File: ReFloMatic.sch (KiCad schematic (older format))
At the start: 33 parts, among them CON1 BARREL_JACK, P1 PROG, P2 THERMOCOUPLE, P3 DOOR_SERVO, P4 OVEN, Q1 MMUN2211, Q2 MMUN2111, Q3 MMUN2111, U1 STM32F030C, U2 MAX31855KASA

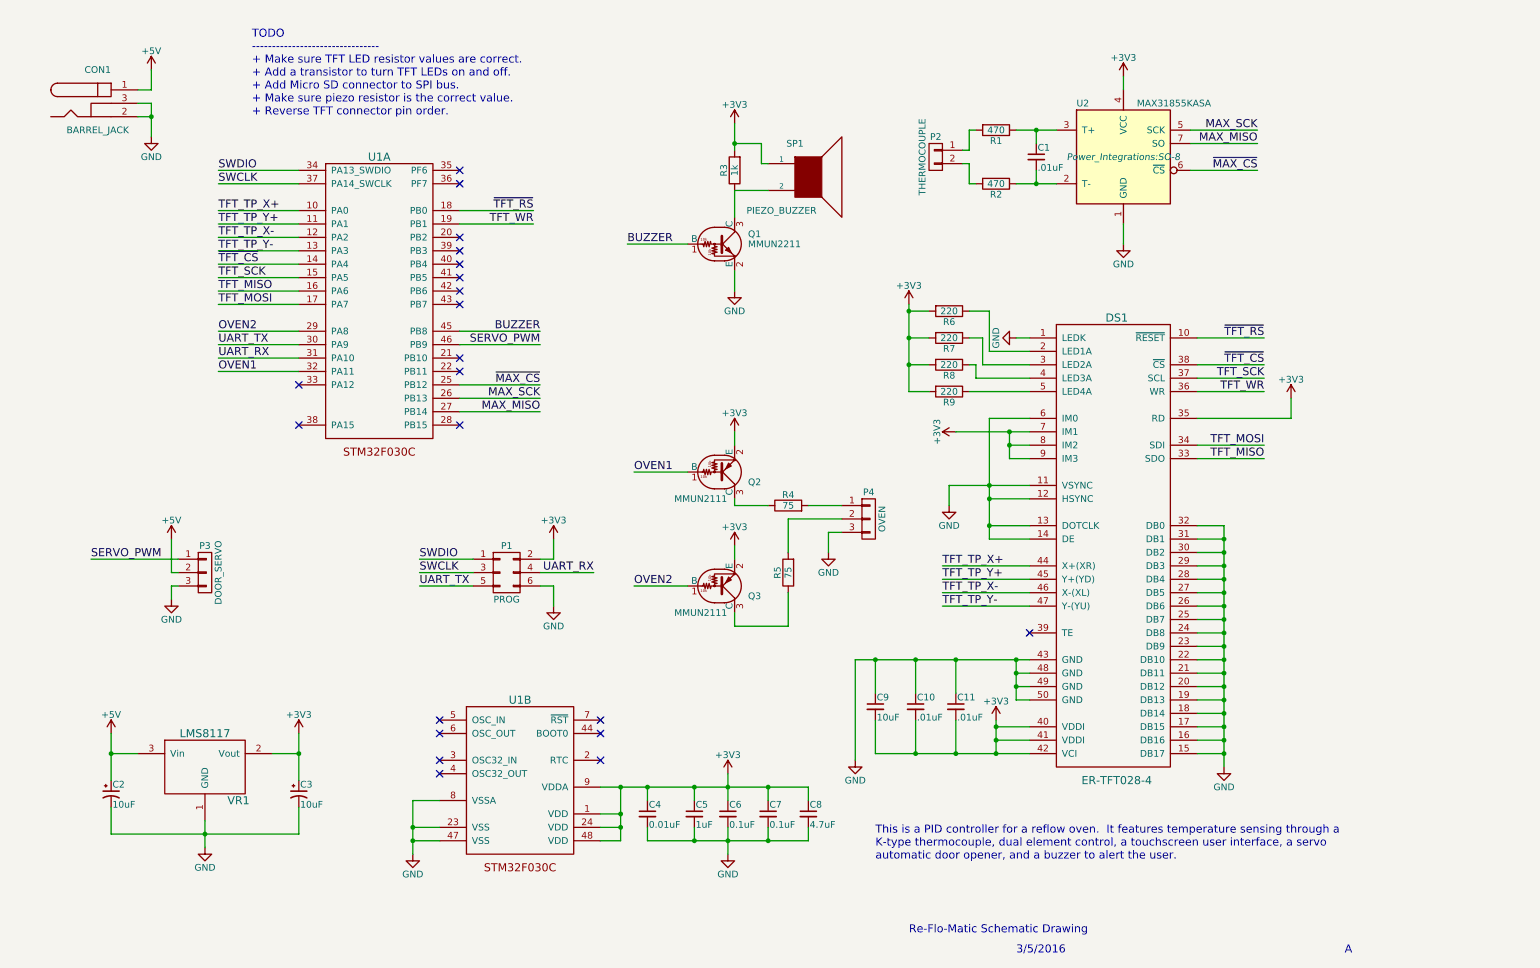
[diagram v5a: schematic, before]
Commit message: Added Micro SD card connector. Changed some component values. Began schematic rev B
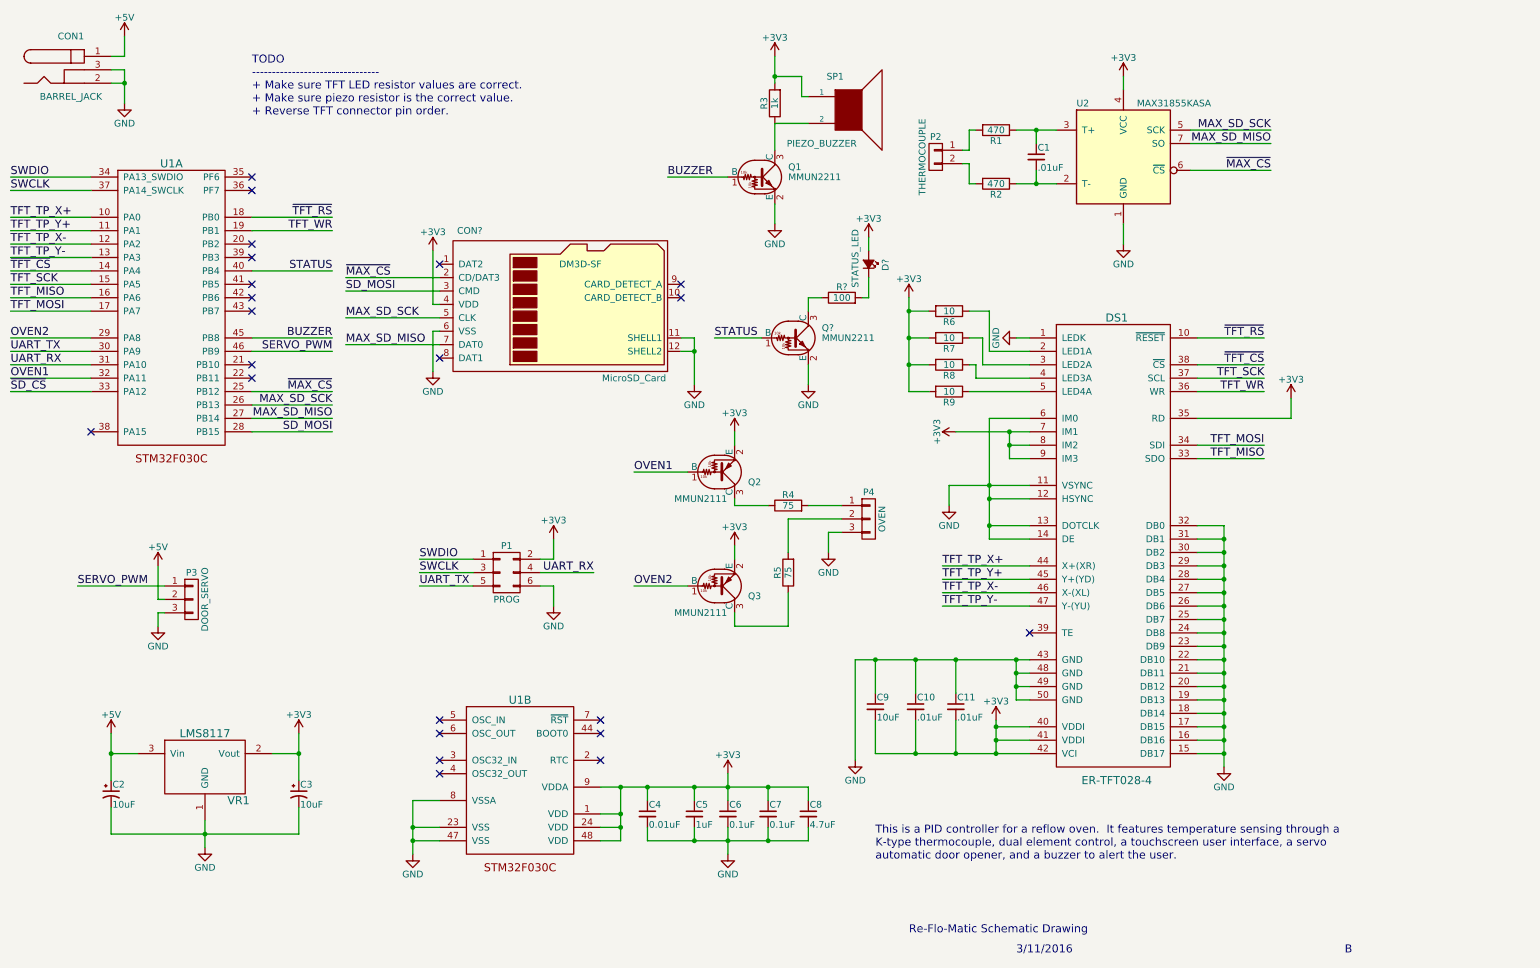
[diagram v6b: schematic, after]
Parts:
- added CON?: MicroSD_Card, DM3D-SF, symbol MicroSD_Card
- added D?: STATUS_LED, symbol Led_Small
- added Q?: MMUN2211, TO_SOT_Packages_SMD:SOT-23_Handsoldering, symbol DTC114E
- added R?: 100, Resistors_SMD:R_0805_HandSoldering, symbol R
- R6, R7, R8, R9: value 220 -> 10
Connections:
- net +3V3: now also CON?.4 (VDD), D?.2 (A)
- net GND: now also CON?.11 (SHELL1), CON?.12 (SHELL2), CON?.6 (VSS), Q?.2 (E)
- net ~MAX_CS: now also CON?.2 (CD/DAT3)
- net SD_MOSI: now reaches U1.28 (PB15)
- net SD_MOSI: now also CON?.3 (CMD)
- net ~SD_CS: now reaches U1.33 (PA12)
- net STATUS: now reaches U1.40 (PB4)
- net STATUS: now also Q?.1 (B)
- net MAX_MISO renamed MAX_SD_MISO
- net MAX_SD_MISO: now also CON?.7 (DAT0)
- net MAX_SCK renamed MAX_SD_SCK
- net MAX_SD_SCK: now also CON?.5 (CLK)
- new net: Q?.3 (C), R?.1
- new net: D?.1 (K), R?.2
- no-connect marks 21 -> 22
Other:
- note added: "3/11/2016"
- note added: "B"
- note added: "TODO\n--------------------------------\n+ Make sure TFT LED resistor values are correct.\n+ Make sure piezo resistor is the correct value.\n+ Reverse TFT connector pin order."
- note removed: "3/5/2016"
- note removed: "A"
- note removed: "TODO\n--------------------------------\n+ Make sure TFT LED resistor values are correct.\n+ Add a transistor to turn TFT LEDs on and off.\n+ Add Micro SD connector to SPI bus.\n+ Make sure piezo resistor is the correct value.\n+ Reverse TFT connector pin order."
- moved on the sheet: CON1, P3, Q1, R3, SP1, U1A

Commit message: Finished Rev. B of schematic.
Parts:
- added R? (x2): 47k, Resistors_SMD:R_0805_HandSoldering, symbol R
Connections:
- net +3V3: now also R?.1, R?.2
- net at CON?.1 (DAT2): now also R?.1
- net at CON?.8 (DAT1): now also R?.2
- no-connect marks 22 -> 20
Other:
- note added: "This is a PID controller for a reflow oven. It features temperature sensing through a\nK-type thermocouple, dual element control, a touchscreen user interface, a servo\nautomatic door opener, a Micro SD slot for storing icons used in the UI and storing\ntemperature profiles, and a buzzer to alert the user."
- note removed: "TODO\n--------------------------------\n+ Make sure TFT LED resistor values are correct.\n+ Make sure piezo resistor is the correct value.\n+ Reverse TFT connector pin order."
- note removed: "This is a PID controller for a reflow oven. It features temperature sensing through a\nK-type thermocouple, dual element control, a touchscreen user interface, a servo\nautomatic door opener, and a buzzer to alert the user."
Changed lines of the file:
@@
 	1    0    0    -1
 $EndComp
-Text Notes 7100 6950 0    60   ~ 0
-This is a PID controller for a reflow oven.  It features temperature sensing through a\nK-type thermocouple, dual element control, a touchscreen user interface, a servo\nautomatic door opener, and a buzzer to alert the user.
+Text Notes 7100 7000 0    60   ~ 0
+This is a PID controller for a reflow oven.  It features temperature sensing through a\nK-type thermocouple, dual element control, a touchscreen user interface, a servo\nautomatic door opener, a Micro SD slot for storing icons used in the UI and storing\ntemperature profiles, and a buzzer to alert the user.
 Text Notes 7350 7500 0    60   ~ 0
 Re-Flo-Matic Schematic Drawing
@@
 Text Notes 10600 7650 0    60   ~ 0
 B
-Text Notes 2450 1400 0    60   ~ 0
-TODO\n--------------------------------\n+ Make sure TFT LED resistor values are correct.\n+ Make sure piezo resistor is the correct value.\n+ Reverse TFT connector pin order.
 Text Label 3050 3750 2    60   ~ 0
 SD_MOSI
@@
 Wire Wire Line
 	3150 2600 3850 2600
-NoConn ~ 3850 2500
 Wire Wire Line
 	3150 3100 3850 3100
-NoConn ~ 3850 3200
 $Comp
 L GND #PWR?
@@
 L +3V3 #PWR?
 U 1 1 56E50399
-P 3800 2400
-F 0 "#PWR?" H 3800 2250 50  0001 C CNN
-F 1 "+3V3" H 3800 2540 50  0000 C CNN
-F 2 "" H 3800 2400 50  0000 C CNN
-F 3 "" H 3800 2400 50  0000 C CNN
-	1    3800 2400
-	1    0    0    -1
-$EndComp
-Wire Wire Line
-	3800 2400 3800 2800
+P 3700 2000
+F 0 "#PWR?" H 3700 1850 50  0001 C CNN
+F 1 "+3V3" H 3700 2140 50  0000 C CNN
+F 2 "" H 3700 2000 50  0000 C CNN
+F 3 "" H 3700 2000 50  0000 C CNN
+	1    3700 2000
+	1    0    0    -1
+$EndComp
+Wire Wire Line
+	3800 2050 3800 2800
 Wire Wire Line
 	3800 2800 3850 2800
+$Comp
+L R R?
+U 1 1 56E5D162
+P 3600 2250
+F 0 "R?" V 3680 2250 50  0000 C CNN
+F 1 "47k" V 3600 2250 50  0000 C CNN
+F 2 "Resistors_SMD:R_0805_HandSoldering" V 3530 2250 50  0001 C CNN
+F 3 "" H 3600 2250 50  0000 C CNN
+	1    3600 2250
+	-1   0    0    1
+$EndComp
+Wire Wire Line
+	3850 2500 3600 2500
+Wire Wire Line
+	3600 2500 3600 2400
+Wire Wire Line
+	3600 2100 3600 2050
+Wire Wire Line
+	3600 2050 3800 2050
+Wire Wire Line
+	3700 2050 3700 2000
+Connection ~ 3700 2050
+$Comp
+L R R?
+U 1 1 56E5D7B9
+P 3500 3250
+F 0 "R?" V 3580 3250 50  0000 C CNN
+F 1 "47k" V 3500 3250 50  0000 C CNN
+F 2 "Resistors_SMD:R_0805_HandSoldering" V 3430 3250 50  0001 C CNN
+F 3 "" H 3500 3250 50  0000 C CNN
+	1    3500 3250
+	0    -1   -1   0
+$EndComp
+$Comp
+L +3V3 #PWR?
+U 1 1 56E5D887
+P 3300 3250
+F 0 "#PWR?" H 3300 3100 50  0001 C CNN
+F 1 "+3V3" H 3300 3390 50  0000 C CNN
+F 2 "" H 3300 3250 50  0000 C CNN
+F 3 "" H 3300 3250 50  0000 C CNN
+	1    3300 3250
+	0    -1   -1   0
+$EndComp
+Wire Wire Line
+	3350 3250 3300 3250
+Wire Wire Line
+	3650 3250 3700 3250
+Wire Wire Line
+	3700 3250 3700 3200
+Wire Wire Line
+	3700 3200 3850 3200
 $EndSCHEMATC

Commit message: Painstakingly created micro sd card footprint and 3D model to match.
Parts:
- C1, C10, C11, C4, C5, C6, C7: footprint Capacitors_SMD:C_0805_HandSoldering -> Capacitors_SMD:C_0805
- CON2: renamed from CON?; footprint DM3D-SF -> SD:DM3D-SF
- D1: renamed from D?; footprint (none) -> LEDs:LED_0805
- DS1: footprint (none) -> TFT:FPC_50
- Q1, Q2, Q3: footprint TO_SOT_Packages_SMD:SOT-23_Handsoldering -> TO_SOT_Packages_SMD:SOT-23
- Q4: renamed from Q?; footprint TO_SOT_Packages_SMD:SOT-23_Handsoldering -> TO_SOT_Packages_SMD:SOT-23
- R1, R2, R3, R4, R5, R6, R7, R8, R9: footprint Resistors_SMD:R_0805_HandSoldering -> Resistors_SMD:R_0805
- R10, R11, R12: renamed from R?; footprint Resistors_SMD:R_0805_HandSoldering -> Resistors_SMD:R_0805
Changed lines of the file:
@@
 F 0 "C1" H 8310 1770 50  0000 L CNN
 F 1 ".01uF" H 8310 1620 50  0000 L CNN
-F 2 "Capacitors_SMD:C_0805_HandSoldering" H 8300 1700 50  0001 C CNN
+F 2 "Capacitors_SMD:C_0805" H 8300 1700 50  0001 C CNN
 F 3 "" H 8300 1700 50  0000 C CNN
 	1    8300 1700
@@
 F 0 "R1" V 8080 1500 50  0000 C CNN
 F 1 "470" V 8000 1500 50  0000 C CNN
-F 2 "Resistors_SMD:R_0805_HandSoldering" V 7930 1500 50  0001 C CNN
+F 2 "Resistors_SMD:R_0805" V 7930 1500 50  0001 C CNN
 F 3 "" H 8000 1500 50  0000 C CNN
 	1    8000 1500
@@
 F 0 "R2" V 8080 1900 50  0000 C CNN
 F 1 "470" V 8000 1900 50  0000 C CNN
-F 2 "Resistors_SMD:R_0805_HandSoldering" V 7930 1900 50  0001 C CNN
+F 2 "Resistors_SMD:R_0805" V 7930 1900 50  0001 C CNN
 F 3 "" H 8000 1900 50  0000 C CNN
 	1    8000 1900
@@
 F 0 "DS1" H 8900 6300 60  0000 C CNN
 F 1 "ER-TFT028-4" H 8900 2850 60  0000 C CNN
-F 2 "" H 8850 6300 60  0001 C CNN
+F 2 "TFT:FPC_50" H 8850 6300 60  0001 C CNN
 F 3 "" H 8850 6300 60  0000 C CNN
 	1    8900 4600
@@
 F 0 "R6" V 7730 2850 50  0000 C CNN
 F 1 "10" V 7650 2850 50  0000 C CNN
-F 2 "Resistors_SMD:R_0805_HandSoldering" V 7580 2850 50  0001 C CNN
+F 2 "Resistors_SMD:R_0805" V 7580 2850 50  0001 C CNN
 F 3 "" H 7650 2850 50  0000 C CNN
 	1    7650 2850
@@
 F 0 "R7" V 7730 3050 50  0000 C CNN
 F 1 "10" V 7650 3050 50  0000 C CNN
-F 2 "Resistors_SMD:R_0805_HandSoldering" V 7580 3050 50  0001 C CNN
+F 2 "Resistors_SMD:R_0805" V 7580 3050 50  0001 C CNN
 F 3 "" H 7650 3050 50  0000 C CNN
 	1    7650 3050
@@
 F 0 "R8" V 7730 3250 50  0000 C CNN
 F 1 "10" V 7650 3250 50  0000 C CNN
-F 2 "Resistors_SMD:R_0805_HandSoldering" V 7580 3250 50  0001 C CNN
+F 2 "Resistors_SMD:R_0805" V 7580 3250 50  0001 C CNN
 F 3 "" H 7650 3250 50  0000 C CNN
 	1    7650 3250
@@
 F 0 "R9" V 7730 3450 50  0000 C CNN
 F 1 "10" V 7650 3450 50  0000 C CNN
-F 2 "Resistors_SMD:R_0805_HandSoldering" V 7580 3450 50  0001 C CNN
+F 2 "Resistors_SMD:R_0805" V 7580 3450 50  0001 C CNN
 F 3 "" H 7650 3450 50  0000 C CNN
 	1    7650 3450
@@
 F 0 "C11" H 7710 5870 50  0000 L CNN
 F 1 ".01uF" H 7710 5720 50  0000 L CNN
-F 2 "Capacitors_SMD:C_0805_HandSoldering" H 7700 5800 50  0001 C CNN
+F 2 "Capacitors_SMD:C_0805" H 7700 5800 50  0001 C CNN
 F 3 "" H 7700 5800 50  0000 C CNN
 	1    7700 5800
@@
 F 0 "C10" H 7410 5870 50  0000 L CNN
 F 1 ".01uF" H 7410 5720 50  0000 L CNN
-F 2 "Capacitors_SMD:C_0805_HandSoldering" H 7400 5800 50  0001 C CNN
+F 2 "Capacitors_SMD:C_0805" H 7400 5800 50  0001 C CNN
 F 3 "" H 7400 5800 50  0000 C CNN
 	1    7400 5800
@@
 F 0 "R3" V 6430 1300 50  0000 C CNN
 F 1 "1k" V 6350 1300 50  0000 C CNN
-F 2 "Resistors_SMD:R_0805_HandSoldering" V 6280 1300 50  0001 C CNN
+F 2 "Resistors_SMD:R_0805" V 6280 1300 50  0001 C CNN
 F 3 "" H 6350 1300 50  0000 C CNN
 	1    6350 1300
@@
 F 0 "R4" V 6530 4300 50  0000 C CNN
 F 1 "75" V 6450 4300 50  0000 C CNN
-F 2 "Resistors_SMD:R_0805_HandSoldering" V 6380 4300 50  0001 C CNN
+F 2 "Resistors_SMD:R_0805" V 6380 4300 50  0001 C CNN
 F 3 "" H 6450 4300 50  0000 C CNN
 	1    6450 4300
@@
 F 0 "R5" V 6530 4800 50  0000 C CNN
 F 1 "75" V 6450 4800 50  0000 C CNN
-F 2 "Resistors_SMD:R_0805_HandSoldering" V 6380 4800 50  0001 C CNN
+F 2 "Resistors_SMD:R_0805" V 6380 4800 50  0001 C CNN
 F 3 "" H 6450 4800 50  0000 C CNN
 	1    6450 4800
@@
 F 0 "C4" H 5410 6670 50  0000 L CNN
 F 1 "0.01uF" H 5410 6520 50  0000 L CNN
-F 2 "Capacitors_SMD:C_0805_HandSoldering" H 5400 6600 50  0001 C CNN
+F 2 "Capacitors_SMD:C_0805" H 5400 6600 50  0001 C CNN
 F 3 "" H 5400 6600 50  0000 C CNN
 	1    5400 6600
@@
 F 0 "C5" H 5760 6670 50  0000 L CNN
 F 1 "1uF" H 5760 6520 50  0000 L CNN
-F 2 "Capacitors_SMD:C_0805_HandSoldering" H 5750 6600 50  0001 C CNN
+F 2 "Capacitors_SMD:C_0805" H 5750 6600 50  0001 C CNN
 F 3 "" H 5750 6600 50  0000 C CNN
 	1    5750 6600
@@
 F 0 "C6" H 6010 6670 50  0000 L CNN
 F 1 "0.1uF" H 6010 6520 50  0000 L CNN
-F 2 "Capacitors_SMD:C_0805_HandSoldering" H 6000 6600 50  0001 C CNN
+F 2 "Capacitors_SMD:C_0805" H 6000 6600 50  0001 C CNN
 F 3 "" H 6000 6600 50  0000 C CNN
 	1    6000 6600
@@
 F 0 "C7" H 6310 6670 50  0000 L CNN
 F 1 "0.1uF" H 6310 6520 50  0000 L CNN
-F 2 "Capacitors_SMD:C_0805_HandSoldering" H 6300 6600 50  0001 C CNN
+F 2 "Capacitors_SMD:C_0805" H 6300 6600 50  0001 C CNN
 F 3 "" H 6300 6600 50  0000 C CNN
 	1    6300 6600
@@
 F 0 "Q1" H 6450 1925 50  0000 L CNN
 F 1 "MMUN2211" H 6450 1850 50  0000 L CNN
-F 2 "TO_SOT_Packages_SMD:SOT-23_Handsoldering" H 6250 1850 50  0001 L CNN
+F 2 "TO_SOT_Packages_SMD:SOT-23" H 6250 1850 50  0001 L CNN
 F 3 "" H 6250 1850 50  0000 L CNN
 	1    6250 1850
@@
 F 0 "Q2" H 6150 4125 50  0000 L CNN
 F 1 "MMUN2111" H 5600 4250 50  0000 L CNN
-F 2 "TO_SOT_Packages_SMD:SOT-23_Handsoldering" H 5950 4050 50  0001 L CNN
+F 2 "TO_SOT_Packages_SMD:SOT-23" H 5950 4050 50  0001 L CNN
 F 3 "" H 5950 4050 50  0000 L CNN
 	1    5950 4050
@@
 F 0 "Q3" H 6150 4975 50  0000 L CNN
 F 1 "MMUN2111" H 5600 5100 50  0000 L CNN
-F 2 "TO_SOT_Packages_SMD:SOT-23_Handsoldering" H 5950 4900 50  0001 L CNN
+F 2 "TO_SOT_Packages_SMD:SOT-23" H 5950 4900 50  0001 L CNN
 F 3 "" H 5950 4900 50  0000 L CNN
 	1    5950 4900
@@
 	650  3450 1250 3450
 $Comp
-L MicroSD_Card CON?
+L MicroSD_Card CON2
 U 1 1 56E3F832
 P 4750 2900
-F 0 "CON?" H 4075 3550 50  0000 C CNN
+F 0 "CON2" H 4075 3550 50  0000 C CNN
 F 1 "MicroSD_Card" H 5300 2450 50  0000 C CNN
-F 2 "DM3D-SF" H 4900 3300 50  0000 C CNN
+F 2 "SD:DM3D-SF" H 4900 3300 50  0001 C CNN
 F 3 "" H 4750 2900 50  0000 C CNN
 	1    4750 2900
@@
 $EndComp
 $Comp
-L DTC114E Q?
+L DTC114E Q4
 U 1 1 56E48E99
 P 6500 3050
-F 0 "Q?" H 6700 3125 50  0000 L CNN
+F 0 "Q4" H 6700 3125 50  0000 L CNN
 F 1 "MMUN2211" H 6700 3050 50  0000 L CNN
-F 2 "TO_SOT_Packages_SMD:SOT-23_Handsoldering" H 6500 3050 50  0001 L CNN
+F 2 "TO_SOT_Packages_SMD:SOT-23" H 6500 3050 50  0001 L CNN
 F 3 "" H 6500 3050 50  0000 L CNN
 	1    6500 3050
@@
 $EndComp
 $Comp
-L GND #PWR?
+L GND #PWR028
 U 1 1 56E48F45
 P 6600 3400
-F 0 "#PWR?" H 6600 3150 50  0001 C CNN
+F 0 "#PWR028" H 6600 3150 50  0001 C CNN
 F 1 "GND" H 6600 3250 50  0000 C CNN
 F 2 "" H 6600 3400 50  0000 C CNN
@@
 	6600 3400 6600 3250
 $Comp
-L GND #PWR?
+L GND #PWR029
 U 1 1 56E4937F
 P 5750 3400
-F 0 "#PWR?" H 5750 3150 50  0001 C CNN
+F 0 "#PWR029" H 5750 3150 50  0001 C CNN
 F 1 "GND" H 5750 3250 50  0000 C CNN
 F 2 "" H 5750 3400 50  0000 C CNN
@@
 NoConn ~ 5650 2750
 $Comp
-L Led_Small D?
+L Led_Small D1
 U 1 1 56E4972B
 P 7050 2500
-F 0 "D?" H 7000 2625 50  0000 L CNN
+F 0 "D1" H 7000 2625 50  0000 L CNN
 F 1 "STATUS_LED" H 6875 2400 50  0000 L CNN
-F 2 "" V 7050 2500 50  0000 C CNN
+F 2 "LEDs:LED_0805" V 7050 2500 50  0001 C CNN
 F 3 "" V 7050 2500 50  0000 C CNN
 	1    7050 2500
@@
 $EndComp
 $Comp
-L R R?
+L R R12
 U 1 1 56E49B4C
 P 6850 2750
-F 0 "R?" V 6930 2750 50  0000 C CNN
+F 0 "R12" V 6930 2750 50  0000 C CNN
 F 1 "100" V 6850 2750 50  0000 C CNN
-F 2 "Resistors_SMD:R_0805_HandSoldering" V 6780 2750 50  0001 C CNN
+F 2 "Resistors_SMD:R_0805" V 6780 2750 50  0001 C CNN
 F 3 "" H 6850 2750 50  0000 C CNN
 	1    6850 2750
@@
 	6600 2750 6600 2850
 $Comp
-L +3V3 #PWR?
+L +3V3 #PWR030
 U 1 1 56E4A30D
 P 7050 2300
-F 0 "#PWR?" H 7050 2150 50  0001 C CNN
+F 0 "#PWR030" H 7050 2150 50  0001 C CNN
 F 1 "+3V3" H 7050 2440 50  0000 C CNN
 F 2 "" H 7050 2300 50  0000 C CNN
@@
 	3150 3100 3850 3100
 $Comp
-L GND #PWR?
+L GND #PWR031
 U 1 1 56E500A3
 P 3800 3300
-F 0 "#PWR?" H 3800 3050 50  0001 C CNN
+F 0 "#PWR031" H 3800 3050 50  0001 C CNN
 F 1 "GND" H 3800 3150 50  0000 C CNN
 F 2 "" H 3800 3300 50  0000 C CNN
@@
 	3800 3000 3800 3300
 $Comp
-L +3V3 #PWR?
+L +3V3 #PWR032
 U 1 1 56E50399
 P 3700 2000
-F 0 "#PWR?" H 3700 1850 50  0001 C CNN
+F 0 "#PWR032" H 3700 1850 50  0001 C CNN
 F 1 "+3V3" H 3700 2140 50  0000 C CNN
 F 2 "" H 3700 2000 50  0000 C CNN
@@
 	3800 2800 3850 2800
 $Comp
-L R R?
+L R R11
 U 1 1 56E5D162
 P 3600 2250
-F 0 "R?" V 3680 2250 50  0000 C CNN
+F 0 "R11" V 3680 2250 50  0000 C CNN
 F 1 "47k" V 3600 2250 50  0000 C CNN
-F 2 "Resistors_SMD:R_0805_HandSoldering" V 3530 2250 50  0001 C CNN
+F 2 "Resistors_SMD:R_0805" V 3530 2250 50  0001 C CNN
 F 3 "" H 3600 2250 50  0000 C CNN
 	1    3600 2250
@@
 Connection ~ 3700 2050
 $Comp
-L R R?
+L R R10
 U 1 1 56E5D7B9
 P 3500 3250
-F 0 "R?" V 3580 3250 50  0000 C CNN
+F 0 "R10" V 3580 3250 50  0000 C CNN
 F 1 "47k" V 3500 3250 50  0000 C CNN
-F 2 "Resistors_SMD:R_0805_HandSoldering" V 3430 3250 50  0001 C CNN
+F 2 "Resistors_SMD:R_0805" V 3430 3250 50  0001 C CNN
 F 3 "" H 3500 3250 50  0000 C CNN
 	1    3500 3250
@@
 $EndComp
 $Comp
-L +3V3 #PWR?
+L +3V3 #PWR033
 U 1 1 56E5D887
 P 3300 3250
-F 0 "#PWR?" H 3300 3100 50  0001 C CNN
+F 0 "#PWR033" H 3300 3100 50  0001 C CNN
 F 1 "+3V3" H 3300 3390 50  0000 C CNN
 F 2 "" H 3300 3250 50  0000 C CNN
